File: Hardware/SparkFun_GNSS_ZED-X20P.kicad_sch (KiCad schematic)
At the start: 70 parts, among them J1 USB_C_Receptacle, J10 U.FL, J11 Conn_01x06, J2 Conn_01x06, J3 Conn_01x09, J4 Qwiic_RA, J5 SMA_Edge, J7 Qwiic_RA, J8 JST_Locking_4, J9 I2C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

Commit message: Post airwire review
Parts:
- removed D11: DF5A5.6LFU, SparkFun-Semiconductor-Standard:SOT-353, symbol SparkFun-DiscreteSemi:D_TVS_ESD_4_HS_3.3V
- removed F1: 6V/0.75A/1.5A, SparkFun-Fuse:1206, symbol SparkFun-Fuse:Fuse 6V/0.75A/1.5A
- removed JP6: UFL, SparkFun-Jumper:Jumper_2_NO_NoSilk, symbol SparkFun-Jumper:SolderJumper_2_Open_No_Silk
- removed R10: 0, SparkFun-Resistor:R_0402_1005Metric, symbol SparkFun-Resistor:0_0402
- added D14: PESD0402, SparkFun-Capacitor:C_0402_1005Metric, symbol SparkFun-DiscreteSemi:D_TVS_0402_14V
- added F1: 6V/0.5A/1A, SparkFun-Fuse:0805, symbol SparkFun-Fuse:Fuse 6V/0.5A/1A
- added JP1: RF, SparkFun-Jumper:Jumper_3_NC-1_Trace, symbol SparkFun-Jumper:SolderJumper_3_Bridged12
- added L2: 33nH, SparkFun-Capacitor:C_0603_1608Metric, symbol SparkFun-Coil:33nH_0603_0.3A
- R6: footprint SparkFun-Resistor:R_0402_1005Metric -> SparkFun-Resistor:R_0603_1608Metric; symbol SparkFun-Resistor:10_0402 -> SparkFun-Resistor:10_0603; PROD_ID RES-16072 -> RES-12581
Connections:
- net VBUS is gone; now on net VUSB: D6.2 (A)
- net 3.3V: now also D8.4 (K3), U5.38 (V_USB); no longer D10.4 (K3)
- net 5V: now also F1.1; no longer D6.1 (K), D7.1 (K)
- net GND: now also D14.1 (A1)
- net RF_IN: now also JP1.2 (B); no longer D3.2 (A2), L1.1
- net RX1/PICO: now also D10.4 (K3); no longer D8.5 (K4)
- net SDA/~{CS}: now also D10.5 (K4); no longer D8.4 (K3)
- net USB_D+: now also U1.1 (I/O1)
- net USB_D-: now also U1.3 (I/O2)
- net VUSB: now also J1.VBUS; no longer U5.38 (V_USB)
- net V_BCKP: now also D8.5 (K4)
- net at J5.1 (In): now also D3.2 (A2), L1.1, JP1.1 (A)
- net at C3.1, L1.2, R6.2: now also L2.2
- net at J10.1 (In): now also D14.2 (A2), JP1.3 (C), L2.1
- new net: D6.1 (K), D7.1 (K), F1.2
- no-connect marks 7 -> 5
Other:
- note added: "Cut and move RF jumper for U.FL connection"
- note removed: "Does R6 need to be 1W? Limit the current to a maximum of 300 mA at the module supply voltage under short circuit conditions, requiring a 10 Ω resistor for a 3 V module supply."
- moved on the sheet: C1, C13, C2, C5, C7, C8, D3, D6, D7, L1, R6, R9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

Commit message: Update to v9.
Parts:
- U1: symbol SparkFun-DiscreteSemi:D_TVS_ESD_USB -> SparkFun-DiscreteSemi:D_TVS_ESD_USB_5V; Rating (none) -> 5VWM/9VC
- U5: footprint SparkFun-GPS:ZED-F9 -> SparkFun-GPS:ZED-F9P_F9T_F9R_X20P; PROD_ID IC-... -> IC-16923
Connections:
- net PPS: now also D12.3 (K2); no longer D12.1 (K1)
- net RX1/PICO: now also D10.3 (K2); no longer D10.4 (K3)
- net RX2: now also D8.1 (K1); no longer D8.3 (K2)
- net SCL/SCK: now also D10.5 (K4); no longer D10.3 (K2)
- net SDA/~{CS}: now also D10.4 (K3); no longer D10.5 (K4)
- net TX2: now also D8.3 (K2); no longer D8.1 (K1)
- net ~{RESET}: now also D12.1 (K1); no longer D12.3 (K2)

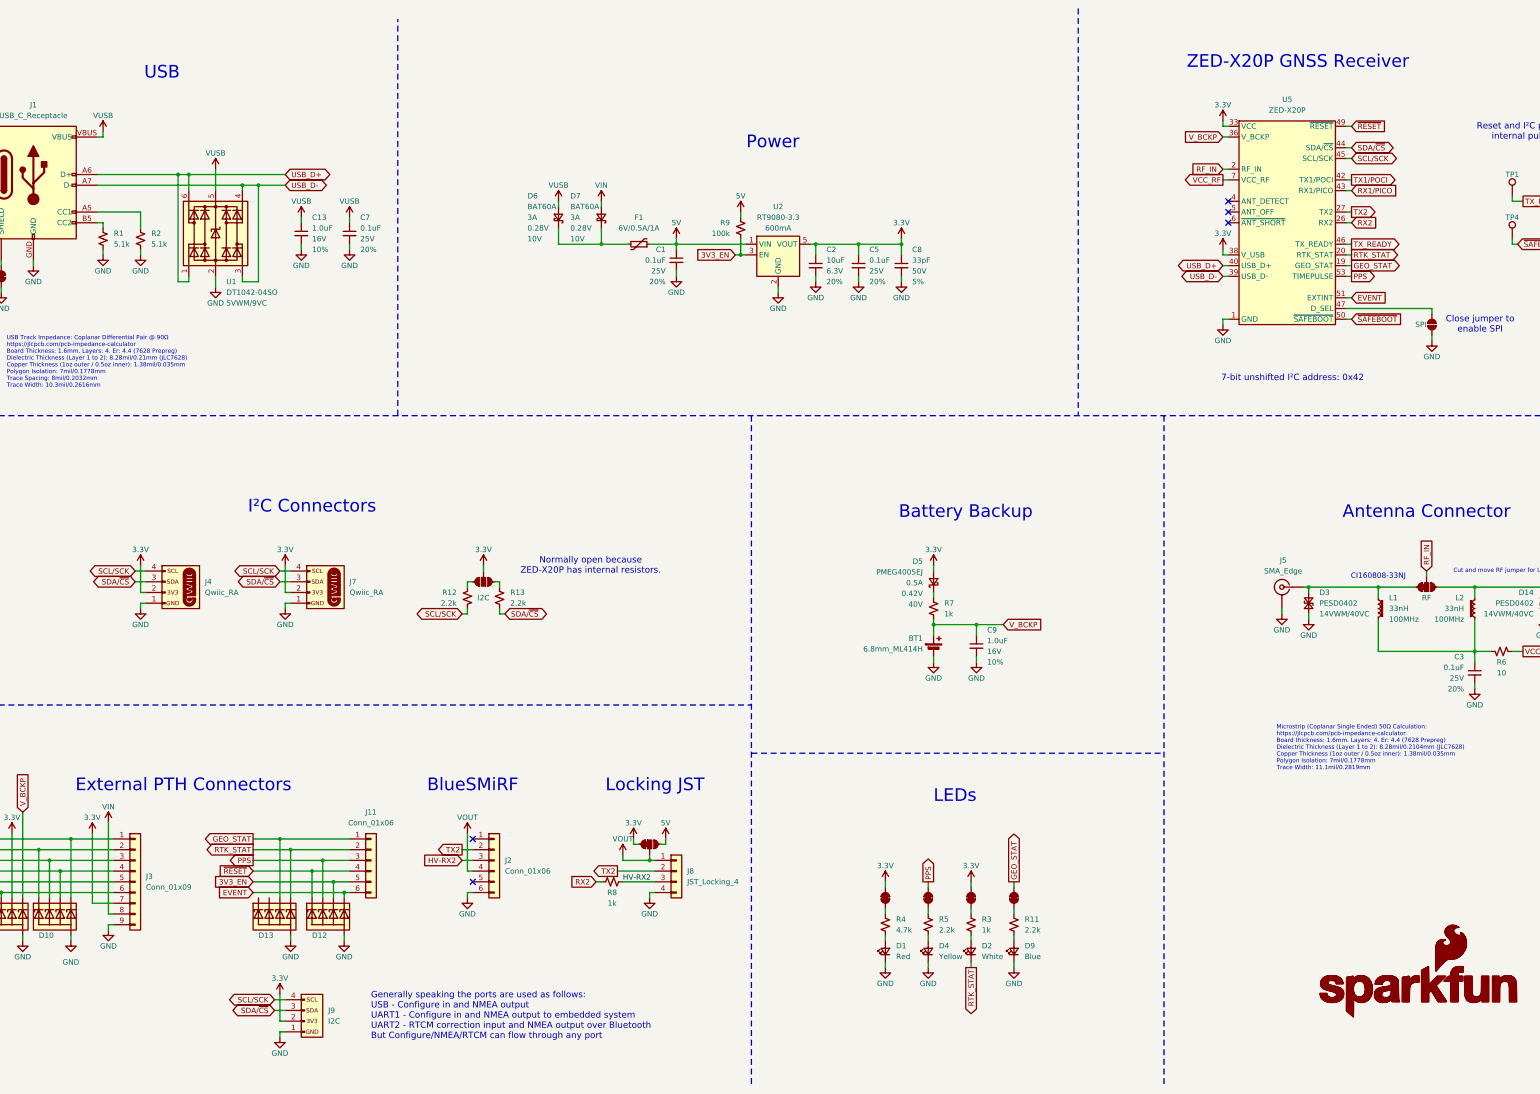
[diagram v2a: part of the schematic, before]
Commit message: Add CH342
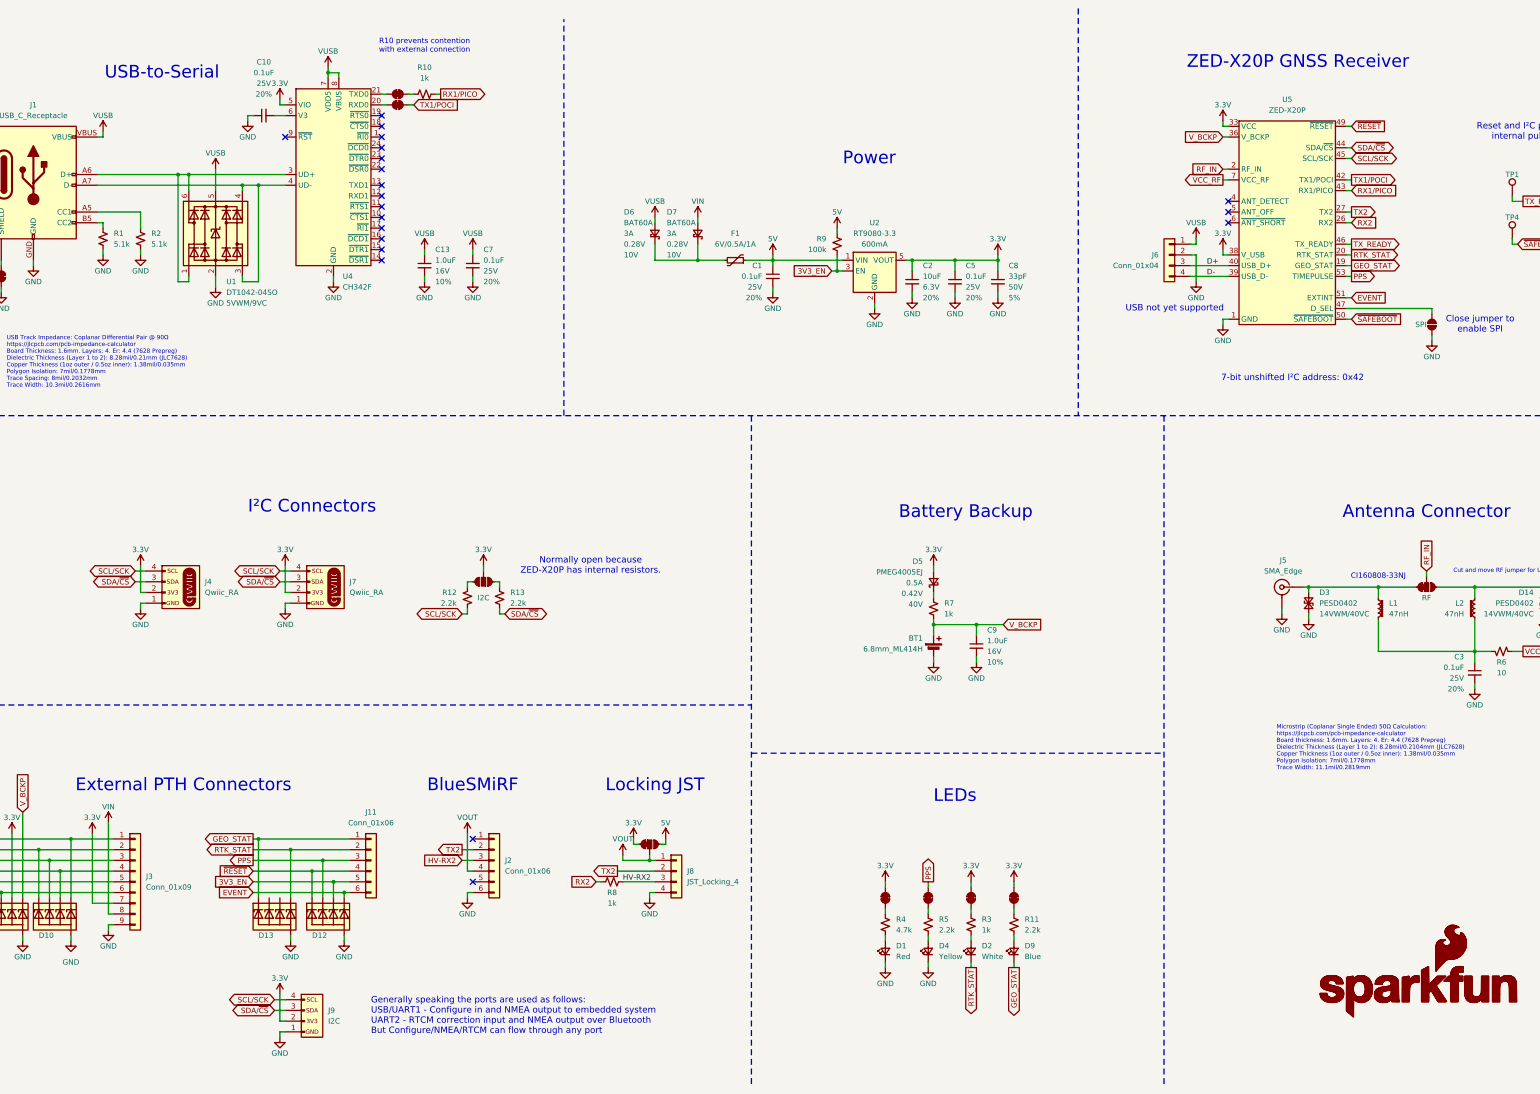
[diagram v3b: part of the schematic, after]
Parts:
- added C10: 0.1uF, SparkFun-Capacitor:C_0603_1608Metric, symbol SparkFun-Capacitor:0.1uF_0603_25V_20%
- added J6: Conn_01x04, SparkFun-Connector:1x04, symbol SparkFun-Connector:Conn_01x04
- added JP11, JP12: ~, SparkFun-Jumper:Jumper_2_NC_Trace, symbol SparkFun-Jumper:SolderJumper_2_Bridged
- added R10: 1k, SparkFun-Resistor:R_0603_1608Metric, symbol SparkFun-Resistor:1k_0603
- added U4: CH342F, SparkFun-Semiconductor-Standard:QFN-24-1EP_4x4mm_P0.5mm_EP2.7x2.7mm, symbol SparkFun-IC-Comm:CH342F
- L1, L2: value 33nH -> 47nH; symbol SparkFun-Coil:33nH_0603_0.3A -> SparkFun-Coil:47nH_0603_0.3A; Frequency 100MHz -> (none); PROD_ID NDUC-13805 -> NDUC-26402; Resistance (none) -> 0.72
- U5: symbol SparkFun-GPS:ZED-F9P -> SparkFun-GPS:ZED-X20P; PROD_ID IC-16923 -> IC-26061
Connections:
- net 3.3V: now also JP8.2 (B), U4.5 (VIO)
- net GEO_STAT: now also D13.1 (K1), D9.1 (K); no longer D13.4 (K3), JP8.2 (B)
- net GND: now also C10.1, J6.2 (Pin_2), U4.2 (GND), U4.25 (GND); no longer D9.1 (K)
- net RX1/PICO: now also R10.1
- net TX1/POCI: now also JP12.2 (B)
- net VUSB: now also J6.1 (Pin_1), U4.7 (VDD5), U4.8 (VBUS)
- net USB_D+: no longer names the net of J1.A6 (D+), J1.B6 (D+), U1.1 (I/O1), U1.6 (I/O4)
- net USB_D+: now also U4.3 (UD+); no longer U5.40 (USB_D+)
- net USB_D-: no longer names the net of J1.A7 (D-), J1.B7 (D-), U1.3 (I/O2), U1.4 (I/O3)
- net USB_D-: now also U4.4 (UD-); no longer U5.39 (USB_D-)
- new net: JP11.1 (A), U4.21 (TXD0)
- new net: JP11.2 (B), R10.2
- new net: JP12.1 (A), U4.20 (RXD0)
- new net: C10.2, U4.6 (V3)
- new net D+: J6.3 (Pin_3), U5.40 (USB_D+)
- new net D-: J6.4 (Pin_4), U5.39 (USB_D-)
- no-connect marks 5 -> 20
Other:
- note added: "Generally speaking the ports are used as follows: USB/UART1 - Configure in and NMEA output to embedded system UART2 - RTCM correction input and NMEA output over Bluetooth But Configure/NMEA/RTCM can flow through any port"
- note added: "R10 prevents contention with external connection"
- note added: "USB not yet supported"
- note added: "USB-to-Serial"
- note removed: "Generally speaking the ports are used as follows: USB - Configure in and NMEA output UART1 - Configure in and NMEA output to embedded system UART2 - RTCM correction input and NMEA output over Bluetooth But Configure/NMEA/RTCM can flow through any port"
- note removed: "USB"
- moved on the sheet: C1, C13, C2, C5, C7, C8, D6, D7, F1, R9, U2
